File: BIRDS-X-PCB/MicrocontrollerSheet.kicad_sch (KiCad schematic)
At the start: 10 parts, among them J401 Conn_02x04_Odd_Even, J402 Conn_01x08, SW401 SW_Push, U401 STM32G031K8Tx, U402 MTT4B-Mini, U403 MT29F2G01ABAGDWB-IT-G_TR, Y401 ECS-2520SMV-080-FN-TR

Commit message: Add more MCU changes
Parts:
- added C404: 10n, Capacitor_SMD:C_1206_3216Metric_Pad1.33x1.80mm_HandSolder, symbol Device:C
- added C405, C407: 100n, Capacitor_SMD:C_1206_3216Metric_Pad1.33x1.80mm_HandSolder, symbol Device:C
- added C406, C408: 4.7u, Capacitor_SMD:C_1206_3216Metric_Pad1.33x1.80mm_HandSolder, symbol Device:C
- added JP401: Jumper_3_Open, Jumper:SolderJumper-3_P1.3mm_Open_RoundedPad1.0x1.5mm_NumberLabels, symbol Jumper:Jumper_3_Open
- added JP402: Jumper_3_Open, Connector_PinHeader_2.54mm:PinHeader_1x03_P2.54mm_Vertical, symbol Jumper:Jumper_3_Open
- added R401, R402: 3.3k, Resistor_SMD:R_1206_3216Metric_Pad1.30x1.75mm_HandSolder, symbol Device:R
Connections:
- net +3V3: now also C404.1, C405.1, C406.1, R402.1
- net +5V: now also C407.1, C408.1
- net GND: now also C404.2, C405.2, C406.2, C407.2, C408.2, R401.2
- net BOOT0: now reaches U401.25 (PA14)
- net BOOT0: now also JP401.2 (C), JP402.2 (C)
- new net: JP401.1 (A), JP402.1 (A), R402.2
- new net: JP401.3 (B), JP402.3 (B), R401.1
- no-connect marks 11 -> 10
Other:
- note added: "Boot Mode: Bridge 1-2: System Mem Bridge 2-3: Main Flash"
- note added: "Decoupling"
- note added: "Decoupling for MCU"
- note added: "Decoupling for MTT4B"
- note added: "Decoupling for SPI"
- moved on the sheet: C402, C403

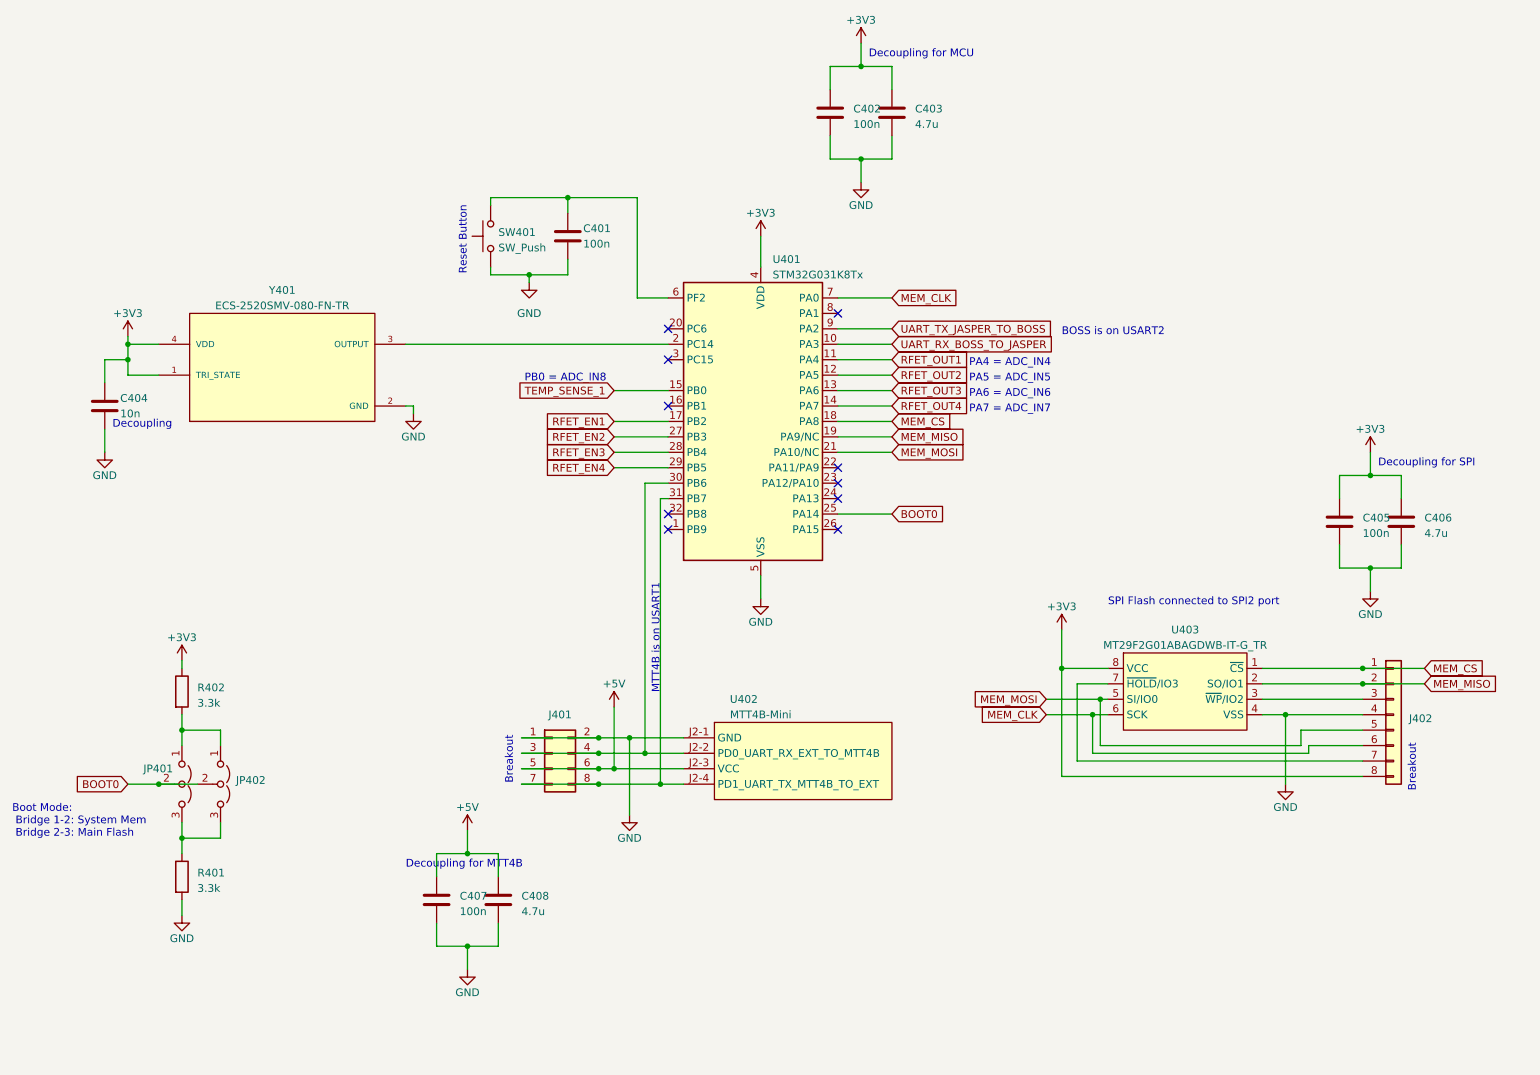
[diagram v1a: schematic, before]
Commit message: Implement oscillator improvements
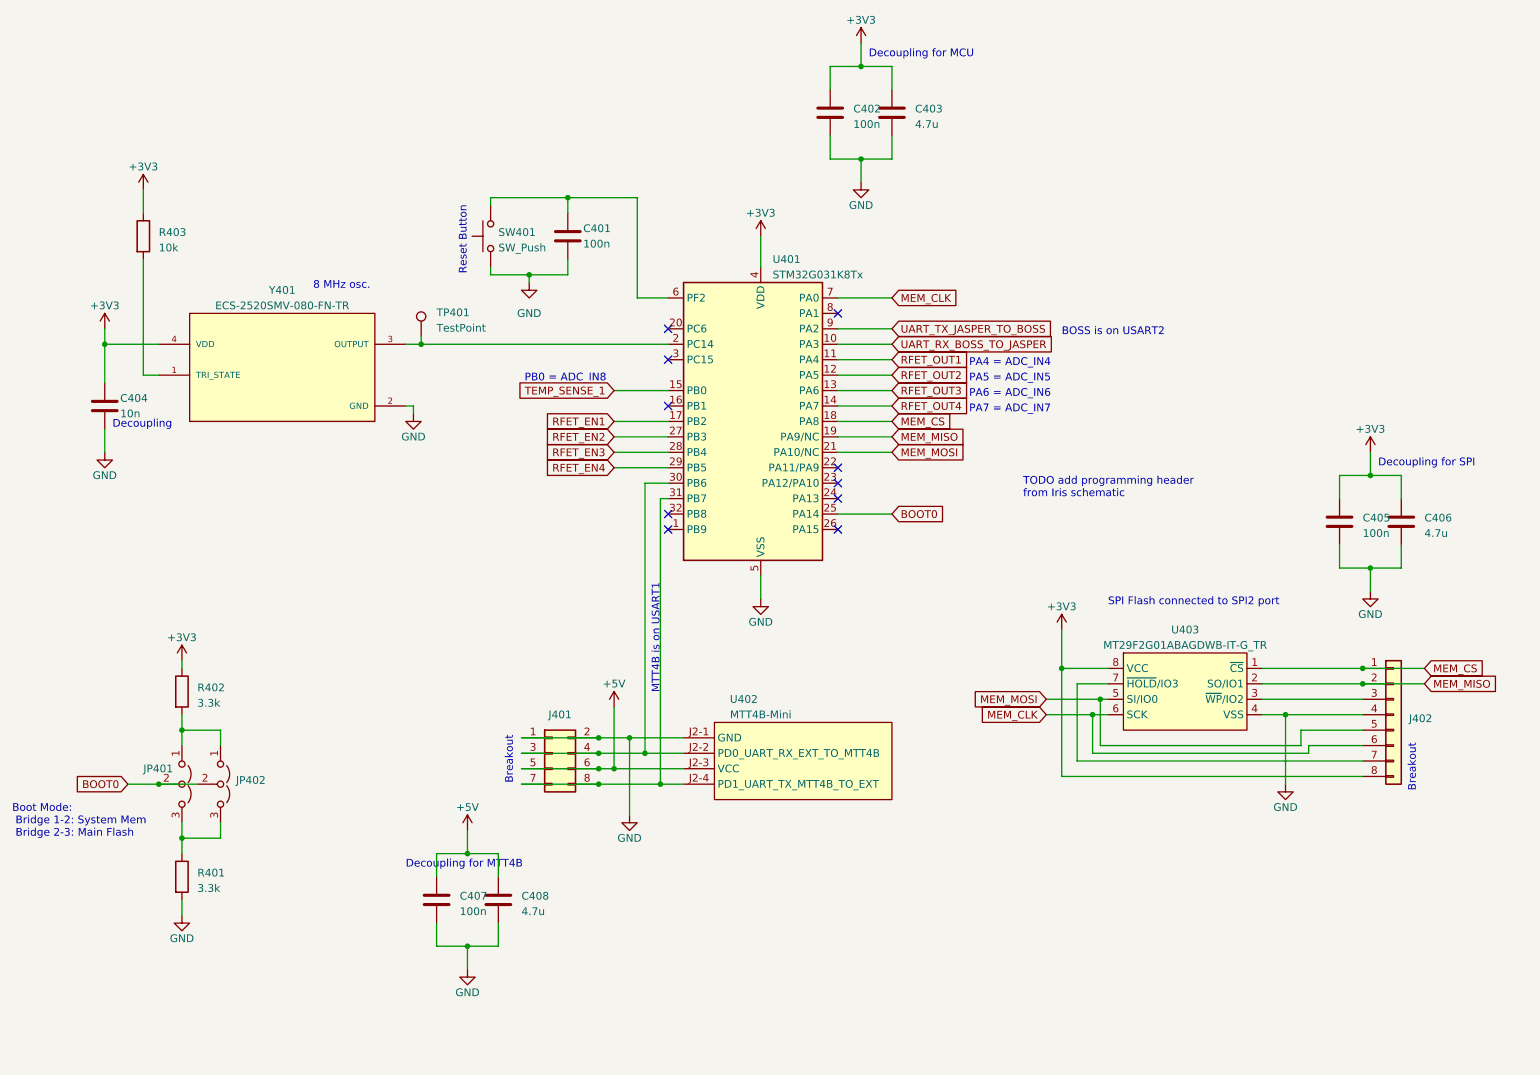
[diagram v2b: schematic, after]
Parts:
- added R403: 10k, Resistor_SMD:R_1206_3216Metric_Pad1.30x1.75mm_HandSolder, symbol Device:R
- added TP401: TestPoint, TestPoint:TestPoint_Pad_D2.5mm, symbol Connector:TestPoint
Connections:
- net +3V3: now also R403.1; no longer Y401.1 (TRI_STATE)
- net at U401.2 (PC14), Y401.3 (OUTPUT): now also TP401.1
- new net: R403.2, Y401.1 (TRI_STATE)
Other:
- note added: "8 MHz osc."
- note added: "TODO add programming header from Iris schematic"
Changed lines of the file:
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@@
   (junction (at 240.03 138.43) (diameter 0) (color 0 0 0 0)
   )
+  (junction (at 85.09 82.55) (diameter 0) (color 0 0 0 0)
+  )
   (junction (at 92.71 181.61) (diameter 0) (color 0 0 0 0)
   )
@@
   (junction (at 157.48 36.83) (diameter 0) (color 0 0 0 0)
   )
-  (junction (at 36.83 85.09) (diameter 0) (color 0 0 0 0)
+  (junction (at 33.02 82.55) (diameter 0) (color 0 0 0 0)
   )
   (junction (at 190.5 135.89) (diameter 0) (color 0 0 0 0)
@@
   )
   (junction (at 240.03 135.89) (diameter 0) (color 0 0 0 0)
-  )
-  (junction (at 36.83 82.55) (diameter 0) (color 0 0 0 0)
   )
   (junction (at 45.72 163.83) (diameter 0) (color 0 0 0 0)
@@
     (stroke (width 0) (type default))
   )
-  (wire (pts (xy 36.83 82.55) (xy 36.83 85.09))
-    (stroke (width 0) (type default))
-  )
   (wire (pts (xy 121.92 105.41) (xy 125.73 105.41))
     (stroke (width 0) (type default))
@@
     (stroke (width 0) (type default))
   )
+  (wire (pts (xy 85.09 81.28) (xy 85.09 82.55))
+    (stroke (width 0) (type default))
+  )
   (wire (pts (xy 52.07 161.29) (xy 52.07 163.83))
     (stroke (width 0) (type default))
@@
     (stroke (width 0) (type default))
   )
+  (wire (pts (xy 33.02 82.55) (xy 33.02 88.9))
+    (stroke (width 0) (type default))
+  )
   (wire (pts (xy 162.56 52.07) (xy 162.56 48.26))
     (stroke (width 0) (type default))
@@
     (stroke (width 0) (type default))
   )
-  (wire (pts (xy 36.83 85.09) (xy 36.83 87.63))
-    (stroke (width 0) (type default))
-  )
-  (wire (pts (xy 82.55 82.55) (xy 125.73 82.55))
+  (wire (pts (xy 82.55 82.55) (xy 85.09 82.55))
+    (stroke (width 0) (type default))
+  )
+  (wire (pts (xy 85.09 82.55) (xy 125.73 82.55))
     (stroke (width 0) (type default))
   )
@@
     (stroke (width 0) (type default))
   )
-  (wire (pts (xy 36.83 81.28) (xy 36.83 82.55))
+  (wire (pts (xy 33.02 80.01) (xy 33.02 82.55))
     (stroke (width 0) (type default))
   )
@@
     (stroke (width 0) (type default))
   )
-  (wire (pts (xy 36.83 87.63) (xy 41.91 87.63))
-    (stroke (width 0) (type default))
-  )
   (wire (pts (xy 45.72 146.05) (xy 45.72 148.59))
     (stroke (width 0) (type default))
   )
-  (wire (pts (xy 33.02 85.09) (xy 36.83 85.09))
-    (stroke (width 0) (type default))
-  )
   (wire (pts (xy 36.83 154.94) (xy 41.91 154.94))
     (stroke (width 0) (type default))
@@
     (stroke (width 0) (type default))
   )
+  (wire (pts (xy 41.91 87.63) (xy 39.37 87.63))
+    (stroke (width 0) (type default))
+  )
   (wire (pts (xy 190.5 135.89) (xy 190.5 153.67))
     (stroke (width 0) (type default))
@@
     (stroke (width 0) (type default))
   )
+  (wire (pts (xy 39.37 87.63) (xy 39.37 68.58))
+    (stroke (width 0) (type default))
+  )
   (wire (pts (xy 102.87 71.12) (xy 102.87 72.39))
     (stroke (width 0) (type default))
@@
     (stroke (width 0) (type default))
   )
+  (wire (pts (xy 39.37 57.15) (xy 39.37 60.96))
+    (stroke (width 0) (type default))
+  )
   (wire (pts (xy 153.67 87.63) (xy 162.56 87.63))
     (stroke (width 0) (type default))
@@
     (stroke (width 0) (type default))
   )
-  (wire (pts (xy 33.02 88.9) (xy 33.02 85.09))
+  (wire (pts (xy 33.02 82.55) (xy 41.91 82.55))
     (stroke (width 0) (type default))
   )
@@
   )
   (wire (pts (xy 116.84 97.79) (xy 125.73 97.79))
-    (stroke (width 0) (type default))
-  )
-  (wire (pts (xy 36.83 82.55) (xy 41.91 82.55))
     (stroke (width 0) (type default))
   )
@@
     (effects (font (size 1.27 1.27)) (justify left bottom))
   )
+  (text "8 MHz osc." (at 67.31 73.66 0)
+    (effects (font (size 1.27 1.27)) (justify left bottom))
+  )
   (text "PA7 = ADC_IN7" (at 175.26 93.98 0)
     (effects (font (size 1.27 1.27)) (justify left bottom))
@@
   )
   (text "Breakout" (at 248.92 156.21 90)
+    (effects (font (size 1.27 1.27)) (justify left bottom))
+  )
+  (text "TODO add programming header\nfrom Iris schematic" (at 184.15 107.95 0)
     (effects (font (size 1.27 1.27)) (justify left bottom))
   )
@@
     (property "Intersheetrefs" "${INTERSHEET_REFS}" (at 190.4423 80.01 0)
       (effects (font (size 1.27 1.27)) (justify left) hide)
+    )
+  )
+  (symbol (lib_id "Device:R") (at 39.37 64.77 0) (unit 1)
+    (in_bom yes) (on_board yes) (dnp no) (fields_autoplaced)
+    (property "Reference" "R403" (at 41.91 64.135 0)
+      (effects (font (size 1.27 1.27)) (justify left))
+    )
+    (property "Value" "10k" (at 41.91 66.675 0)
+      (effects (font (size 1.27 1.27)) (justify left))
+    )
+    (property "Footprint" "Resistor_SMD:R_1206_3216Metric_Pad1.30x1.75mm_HandSolder" (at 37.592 64.77 90)
+      (effects (font (size 1.27 1.27)) hide)
+    )
+    (property "Datasheet" "~" (at 39.37 64.77 0)
+      (effects (font (size 1.27 1.27)) hide)
+    )
+    (pin "1")
+    (pin "2")
+    (instances
+      (project "BIRDS-X-PCB"
+        (path "/c2796b15-795a-4d6e-ad4b-0ba87ded4bc9/d490f402-3a4d-40a5-b165-30c74c6560b7"
+          (reference "R403") (unit 1)
+        )
+      )
     )
   )
@@
     )
   )
-  (symbol (lib_id "power:+3V3") (at 36.83 81.28 0) (unit 1)
-    (in_bom yes) (on_board yes) (dnp no) (fields_autoplaced)
-    (property "Reference" "#PWR0401" (at 36.83 85.09 0)
-      (effects (font (size 1.27 1.27)) hide)
-    )
-    (property "Value" "+3V3" (at 36.83 77.47 0)
-      (effects (font (size 1.27 1.27)))
-    )
-    (property "Footprint" "" (at 36.83 81.28 0)
-      (effects (font (size 1.27 1.27)) hide)
-    )
-    (property "Datasheet" "" (at 36.83 81.28 0)
+  (symbol (lib_id "Connector:TestPoint") (at 85.09 81.28 0) (unit 1)
+    (in_bom yes) (on_board yes) (dnp no) (fields_autoplaced)
+    (property "Reference" "TP401" (at 87.63 77.343 0)
+      (effects (font (size 1.27 1.27)) (justify left))
+    )
+    (property "Value" "TestPoint" (at 87.63 79.883 0)
+      (effects (font (size 1.27 1.27)) (justify left))
+    )
+    (property "Footprint" "TestPoint:TestPoint_Pad_D2.5mm" (at 90.17 81.28 0)
+      (effects (font (size 1.27 1.27)) hide)
+    )
+    (property "Datasheet" "~" (at 90.17 81.28 0)
+      (effects (font (size 1.27 1.27)) hide)
+    )
+    (pin "1")
+    (instances
+      (project "BIRDS-X-PCB"
+        (path "/c2796b15-795a-4d6e-ad4b-0ba87ded4bc9/d490f402-3a4d-40a5-b165-30c74c6560b7"
+          (reference "TP401") (unit 1)
+        )
+      )
+    )
+  )
+  (symbol (lib_id "power:+3V3") (at 33.02 80.01 0) (unit 1)
+    (in_bom yes) (on_board yes) (dnp no) (fields_autoplaced)
+    (property "Reference" "#PWR0401" (at 33.02 83.82 0)
+      (effects (font (size 1.27 1.27)) hide)
+    )
+    (property "Value" "+3V3" (at 33.02 76.2 0)
+      (effects (font (size 1.27 1.27)))
+    )
+    (property "Footprint" "" (at 33.02 80.01 0)
+      (effects (font (size 1.27 1.27)) hide)
+    )
+    (property "Datasheet" "" (at 33.02 80.01 0)
       (effects (font (size 1.27 1.27)) hide)
     )
@@
         )
       )
+    )
+  )
+  (symbol (lib_id "power:+3V3") (at 39.37 57.15 0) (unit 1)
+    (in_bom yes) (on_board yes) (dnp no) (fields_autoplaced)
+    (property "Reference" "#PWR0419" (at 39.37 60.96 0)
+      (effects (font (size 1.27 1.27)) hide)
+    )
+    (property "Value" "+3V3" (at 39.37 53.34 0)
+      (effects (font (size 1.27 1.27)))
+    )
+    (property "Footprint" "" (at 39.37 57.15 0)
+      (effects (font (size 1.27 1.27)) hide)
+    )
+    (property "Datasheet" "" (at 39.37 57.15 0)
+      (effects (font (size 1.27 1.27)) hide)
+    )
+    (pin "1")
+    (instances
+      (project "BIRDS-X-PCB"
+        (path "/c2796b15-795a-4d6e-ad4b-0ba87ded4bc9/d490f402-3a4d-40a5-b165-30c74c6560b7"
+          (reference "#PWR0419") (unit 1)
+        )
+      )

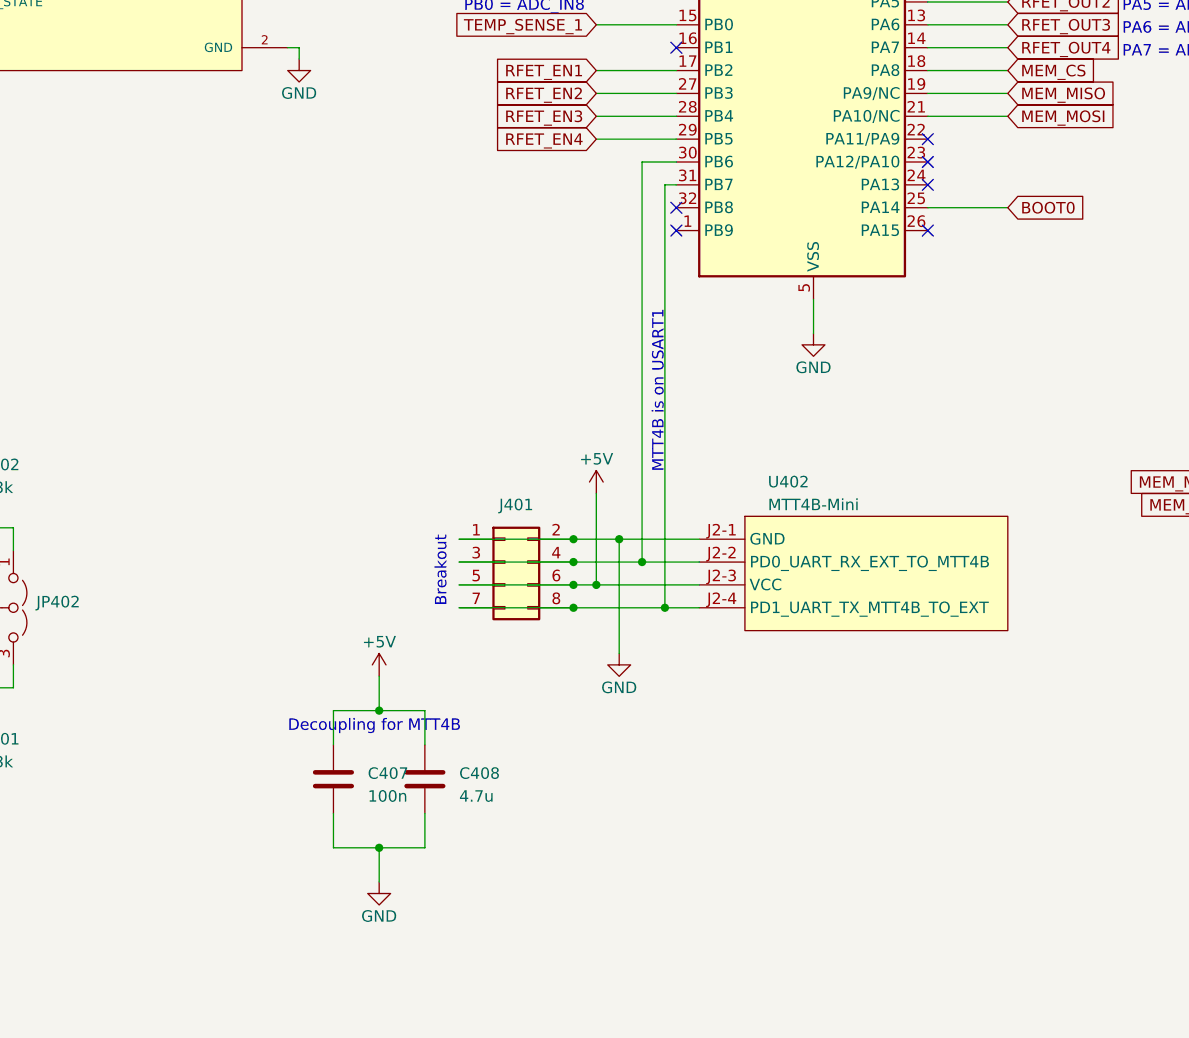
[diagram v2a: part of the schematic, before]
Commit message: Add logic level converters, etc.
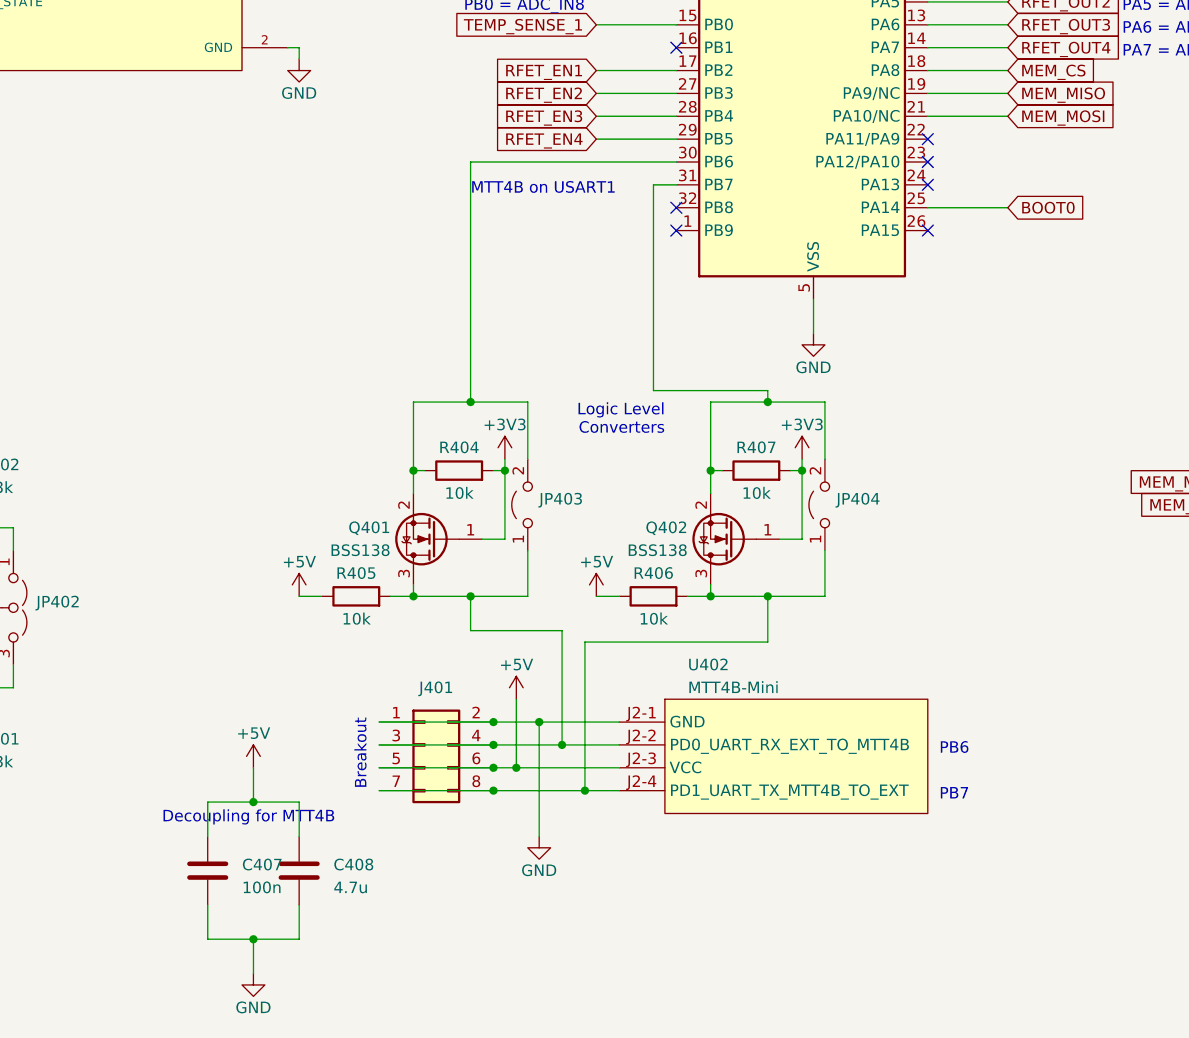
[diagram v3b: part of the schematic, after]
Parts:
- added JP403, JP404: Jumper_2_Open, symbol Jumper:Jumper_2_Open
- added Q401, Q402: BSS138, Package_TO_SOT_SMD:SOT-23, symbol Transistor_FET:BSS138
- added R404, R405, R406, R407: 10k, symbol Device:R
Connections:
- net +3V3: now also Q401.1 (G), Q402.1 (G), R404.2, R407.2
- net +5V: now also R405.1, R406.1
- net at J401.3 (Pin_3), J401.4 (Pin_4), U402.J2-2 (PD0_UART_RX_EXT_TO_MTT4B): now also JP403.1 (A), Q401.3 (D), R405.2; no longer U401.30 (PB6)
- net at J401.7 (Pin_7), J401.8 (Pin_8), U402.J2-4 (PD1_UART_TX_MTT4B_TO_EXT): now also JP404.1 (A), Q402.3 (D), R406.2; no longer U401.31 (PB7)
- new net: JP403.2 (B), Q401.2 (S), R404.1, U401.30 (PB6)
- new net: JP404.2 (B), Q402.2 (S), R407.1, U401.31 (PB7)
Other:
- note added: "Logic Level Converters"
- note added: "MTT4B on USART1"
- note added: "PB6"
- note added: "PB7"
- note removed: "MTT4B is on USART1"
- moved on the sheet: C407, C408, J401, U402
